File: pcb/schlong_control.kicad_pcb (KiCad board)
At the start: 2 copper layers, 50 x 50 mm, 37 parts, among them P1 Power Connector (120V AC), P2 Input, P3 Output, U1 74HC595, U2 MOC3063M, U3 MOC3063M, U4 MOC3063M, U5 MOC3063M, U6 MOC3063M, U7 LM7805

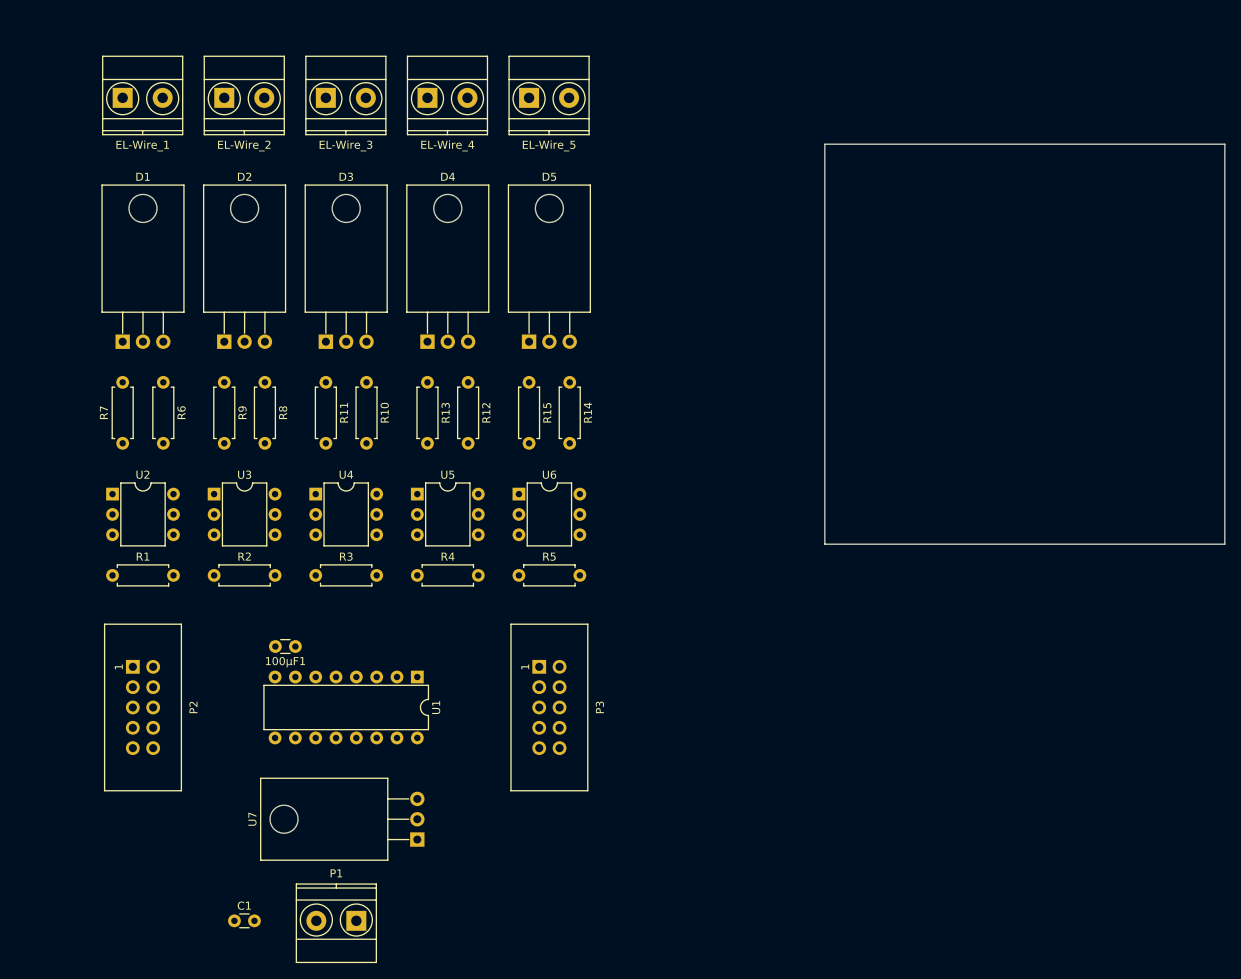
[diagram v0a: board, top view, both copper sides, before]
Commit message: make pcb more compact
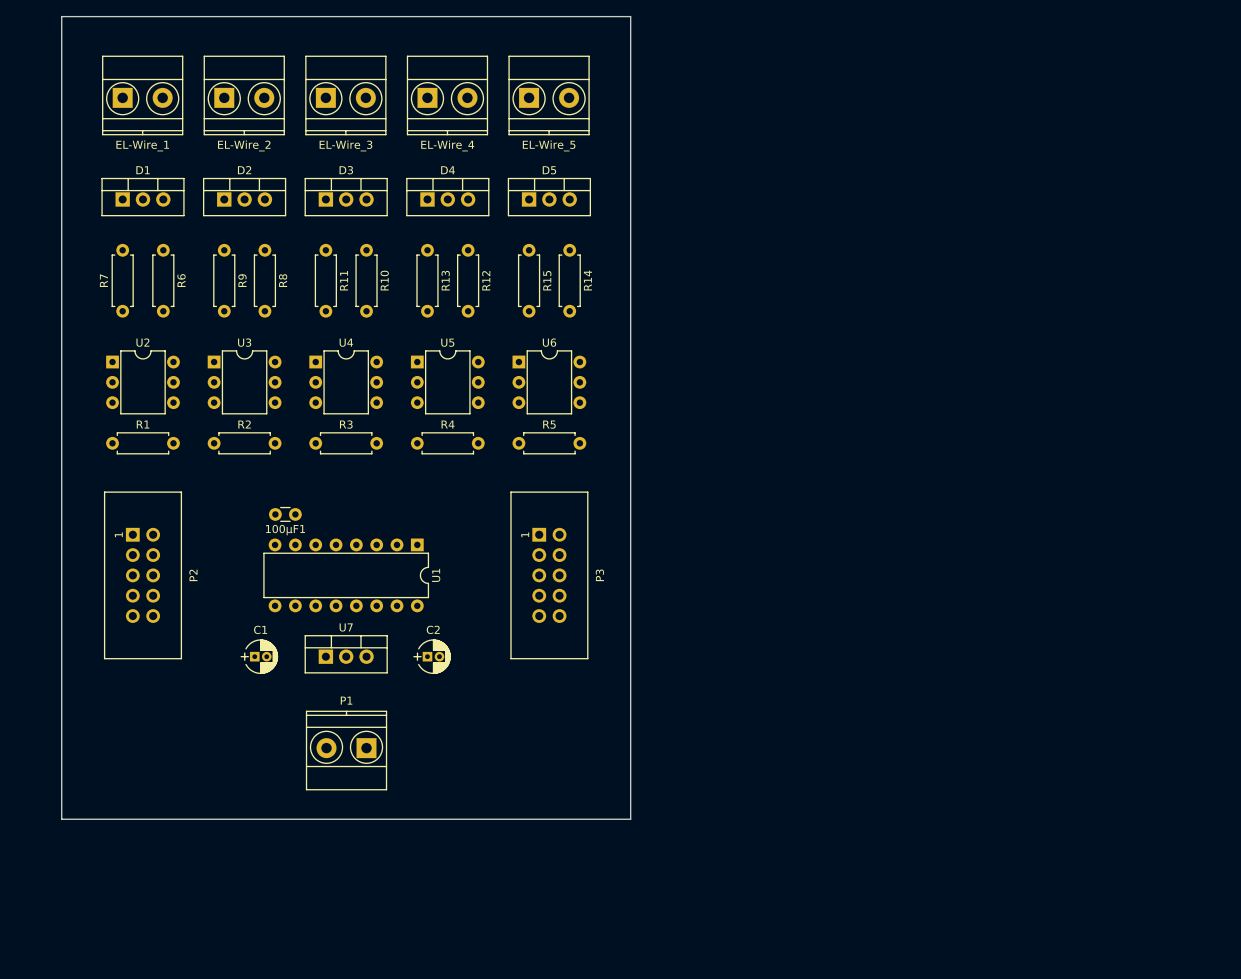
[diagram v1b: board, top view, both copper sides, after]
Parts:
- added C2: 0.1uF, Capacitors_THT:CP_Radial_D4.0mm_P1.50mm, F.Cu at (100.3, 99.1)
- C1: value 0.22µF -> 0.33µF; footprint Capacitors_THT:C_Disc_D3.0mm_W1.6mm_P2.50mm -> Capacitors_THT:CP_Radial_D4.0mm_P1.50mm
- D1, D2, D3, D4, D5, U7: footprint TO_SOT_Packages_THT:TO-220_Horizontal -> TO_SOT_Packages_THT:TO-220_Vertical
- moved C1 33.1 mm to (78.7, 99.1)
- moved U7 25.6 mm to (87.6, 99.1), turned to 0 degrees
- moved P1 21.6 mm to (92.7, 110.5)
- moved D1 17.8 mm to (62.2, 41.9)
- moved D2 17.8 mm to (74.9, 41.9)
- moved D3 17.8 mm to (87.6, 41.9)
- moved D4 17.8 mm to (100.3, 41.9)
- moved D5 17.8 mm to (113.0, 41.9)
- moved 100µF1 16.5 mm to (83.8, 81.3)
- moved P2 16.5 mm to (63.5, 83.8)
- moved P3 16.5 mm to (114.3, 83.8)
- moved R1 16.5 mm to (61.0, 72.4)
- moved R2 16.5 mm to (73.7, 72.4)
- moved R3 16.5 mm to (86.4, 72.4)
- moved R4 16.5 mm to (99.1, 72.4)
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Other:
- board size 50 x 50 mm -> 71.1 x 100.3 mm

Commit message: shinkify pcb even more + little fixes
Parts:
- EL-Wire_1, EL-Wire_2, EL-Wire_3, EL-Wire_4, EL-Wire_5: footprint Connectors_Terminal_Blocks:TerminalBlock_Pheonix_MKDS1.5-2pol -> Connectors:PINHEAD1-2
- moved C1 6.35 mm to (78.7, 92.7)
- moved C2 6.35 mm to (100.3, 92.7)
- moved U1 6.35 mm to (99.1, 78.7)
- moved U7 6.35 mm to (87.6, 92.7)
- moved R10 6.35 mm to (92.7, 41.9)
- moved R11 6.35 mm to (87.6, 41.9)
- moved R12 6.35 mm to (105.4, 41.9)
- moved R13 6.35 mm to (100.3, 41.9)
- moved R14 6.35 mm to (118.1, 41.9)
- moved R15 6.35 mm to (113.0, 41.9)
- moved R6 6.35 mm to (67.3, 41.9)
- moved R7 6.35 mm to (62.2, 49.5)
- moved R8 6.35 mm to (80.0, 41.9)
- moved R9 6.35 mm to (74.9, 41.9)
- moved 100µF1 6.35 mm to (83.8, 74.9)
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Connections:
- U1 pad 5: (no net) -> Net-(U1-Pad5)
- U1 pad 6: (no net) -> Net-(U1-Pad6)
- U1 pad 7: (no net) -> Net-(U1-Pad7)
- U2 pad 3: (no net) -> Net-(U2-Pad3)
- U2 pad 5: (no net) -> Net-(U2-Pad5)
- U3 pad 3: (no net) -> Net-(U3-Pad3)
- U3 pad 5: (no net) -> Net-(U3-Pad5)
- U4 pad 3: (no net) -> Net-(U4-Pad3)
- U4 pad 5: (no net) -> Net-(U4-Pad5)
- U5 pad 3: (no net) -> Net-(U5-Pad3)
- U5 pad 5: (no net) -> Net-(U5-Pad5)
- U6 pad 3: (no net) -> Net-(U6-Pad3)
- U6 pad 5: (no net) -> Net-(U6-Pad5)
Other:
- board size 71.1 x 100.3 mm -> 71.1 x 95.2 mm

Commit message: routed pcb
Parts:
- moved R7 7.53 mm to (62.2, 42.0), turned to 270 degrees
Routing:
- net /AC_P: track 0.00 -> 194.1 mm
- net /AC_N: track 0.00 -> 193.0 mm
- net GND: track 0.00 -> 182.4 mm
- net +12V: track 0.00 -> 81.3 mm
- net /SCK: track 0.00 -> 76.5 mm, vias 0 -> 4
- net /~LATCH: track 0.00 -> 58.4 mm, vias 0 -> 2
- net VCC: track 0.00 -> 54.6 mm
- net Net-(R1-Pad2): track 0.00 -> 40.4 mm
- net /~QH: track 0.00 -> 38.9 mm, vias 0 -> 2
- net Net-(R5-Pad2): track 0.00 -> 35.6 mm, vias 0 -> 1
- net /MOSI: track 0.00 -> 34.2 mm, vias 0 -> 1
- net Net-(D5-Pad3): track 0.00 -> 32.5 mm
- net Net-(D4-Pad3): track 0.00 -> 32.3 mm
- net Net-(D2-Pad3): track 0.00 -> 32.2 mm
- net Net-(D3-Pad3): track 0.00 -> 32.0 mm
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
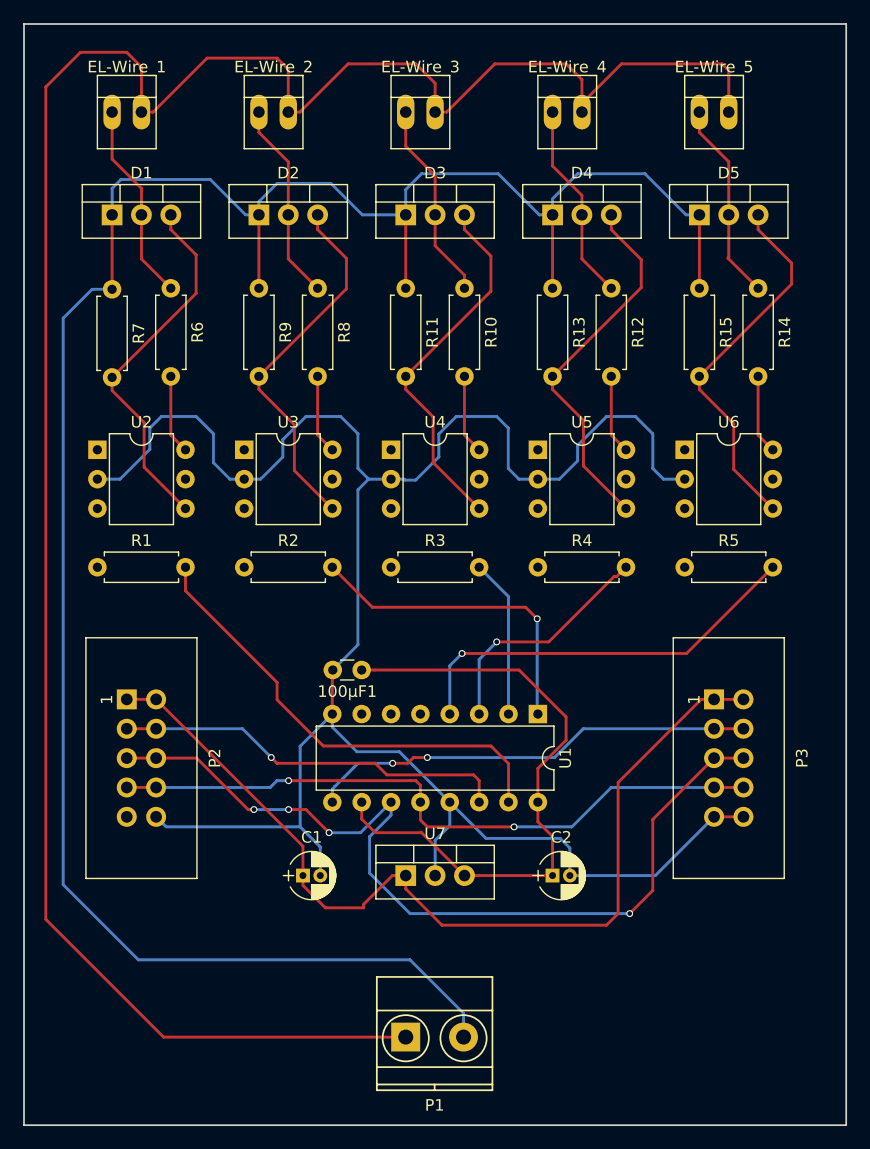
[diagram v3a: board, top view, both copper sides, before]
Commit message: redo routing (seperate logic voltage from AC voltage)
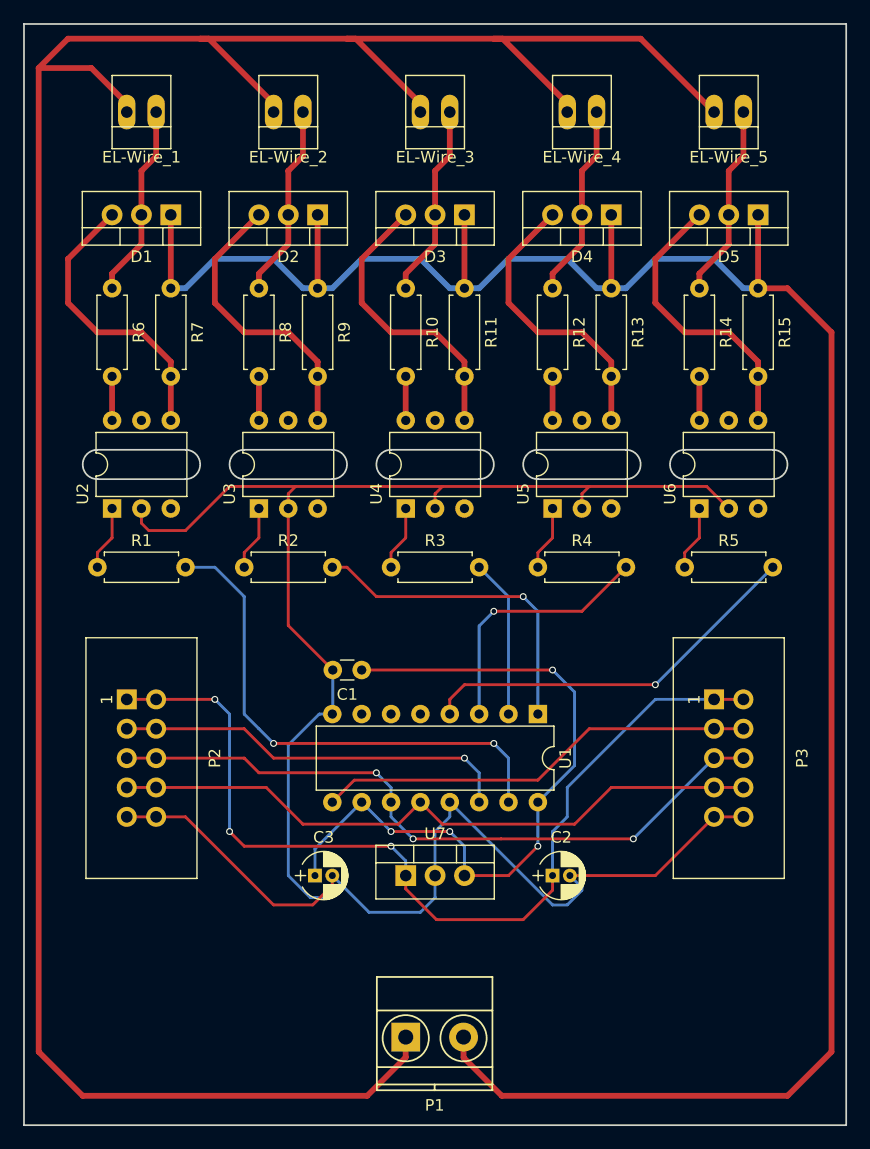
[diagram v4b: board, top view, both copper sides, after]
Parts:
- removed 100µF1: Bypass, Capacitors_THT:C_Disc_D3.0mm_W1.6mm_P2.50mm
- added C3: 0.1uF, Capacitors_ThroughHole:CP_Radial_D4.0mm_P1.50mm, F.Cu at (79.8, 92.7)
- C1: value 0.33µF -> 100nF; footprint Capacitors_THT:CP_Radial_D4.0mm_P1.50mm -> Capacitors_ThroughHole:C_Disc_D3.0mm_W1.6mm_P2.50mm
- C2: value 0.1uF -> 0.33µF; footprint Capacitors_THT:CP_Radial_D4.0mm_P1.50mm -> Capacitors_ThroughHole:CP_Radial_D4.0mm_P1.50mm
- moved C1 18.5 mm to (83.8, 74.9), turned to 180 degrees
- moved U3 5.24 mm to (74.9, 61.0), turned to 90 degrees
- moved U2 5.24 mm to (62.2, 61.0), turned to 90 degrees
- moved U4 5.24 mm to (87.6, 61.0), turned to 90 degrees
- moved U5 5.24 mm to (100.3, 61.0), turned to 90 degrees
- moved U6 5.24 mm to (113.0, 61.0), turned to 90 degrees
- moved R7 5.08 mm to (67.3, 41.9)
- moved D1 5.08 mm to (67.3, 35.6), turned to 180 degrees
- moved R6 5.08 mm to (62.2, 41.9)
- moved D2 5.08 mm to (80.0, 35.6), turned to 180 degrees
- moved D3 5.08 mm to (92.7, 35.6), turned to 180 degrees
- moved D4 5.08 mm to (105.4, 35.6), turned to 180 degrees
- moved D5 5.08 mm to (118.1, 35.6), turned to 180 degrees
- moved R10 5.08 mm to (87.6, 41.9)
- moved R11 5.08 mm to (92.7, 41.9)
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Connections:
- C1 pad 1: +12V -> VCC
- C2 pad 1: VCC -> +12V
- U1 pad 5: Net-(U1-Pad5) -> (no net)
- U1 pad 6: Net-(U1-Pad6) -> (no net)
- U1 pad 7: Net-(U1-Pad7) -> (no net)
- U2 pad 3: Net-(U2-Pad3) -> (no net)
- U2 pad 5: Net-(U2-Pad5) -> (no net)
- U3 pad 3: Net-(U3-Pad3) -> (no net)
- U3 pad 5: Net-(U3-Pad5) -> (no net)
- U4 pad 3: Net-(U4-Pad3) -> (no net)
- U4 pad 5: Net-(U4-Pad5) -> (no net)
- U5 pad 3: Net-(U5-Pad3) -> (no net)
- U5 pad 5: Net-(U5-Pad5) -> (no net)
- U6 pad 3: Net-(U6-Pad3) -> (no net)
- U6 pad 5: Net-(U6-Pad5) -> (no net)
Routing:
- net /AC_P: track 194.1 -> 221.5 mm
- net /SCK: track 76.5 -> 60.6 mm, vias 4 -> 3
- net VCC: track 54.6 -> 62.3 mm, vias 0 -> 4
- net Net-(D5-Pad3): track 32.5 -> 25.3 mm
- net Net-(D4-Pad3): track 32.3 -> 25.3 mm
- net Net-(D2-Pad3): track 32.2 -> 25.3 mm
- net Net-(D3-Pad3): track 32.0 -> 25.3 mm
- net Net-(D1-Pad3): track 31.9 -> 25.3 mm
- net /AC_N: track 193.0 -> 198.9 mm
- net Net-(R2-Pad1): track 0.00 -> 5.61 mm
- net Net-(R5-Pad1): track 0.00 -> 5.61 mm
- net Net-(R4-Pad1): track 0.00 -> 5.61 mm
- net Net-(R3-Pad1): track 0.00 -> 5.61 mm
- net Net-(R1-Pad1): track 0.00 -> 5.61 mm
- net Net-(R1-Pad2): track 40.4 -> 44.5 mm, vias 0 -> 2
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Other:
- outline, holes or cut-outs redrawn

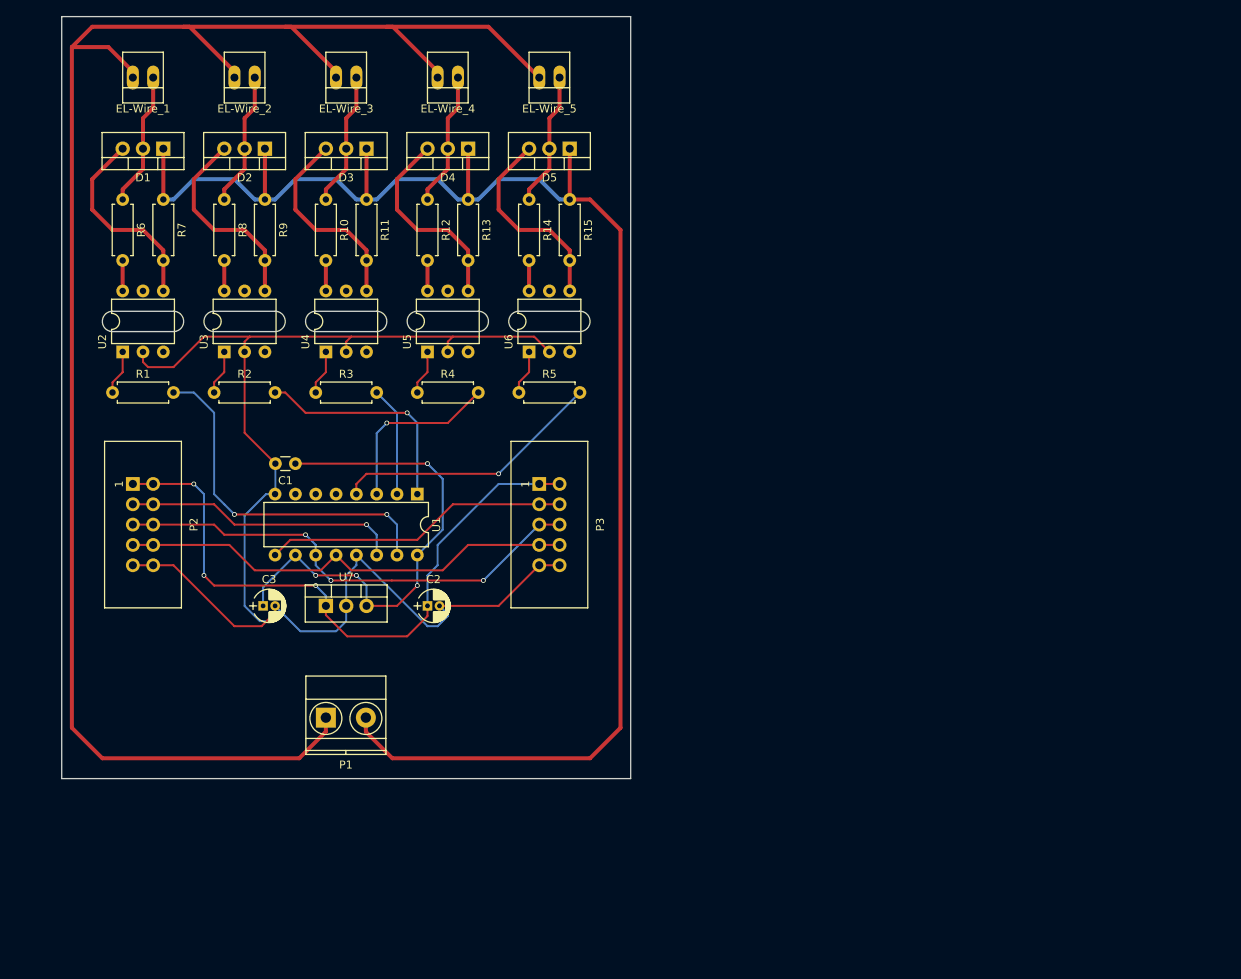
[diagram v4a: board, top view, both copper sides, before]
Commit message: pcb: improve seperation of low / high voltages
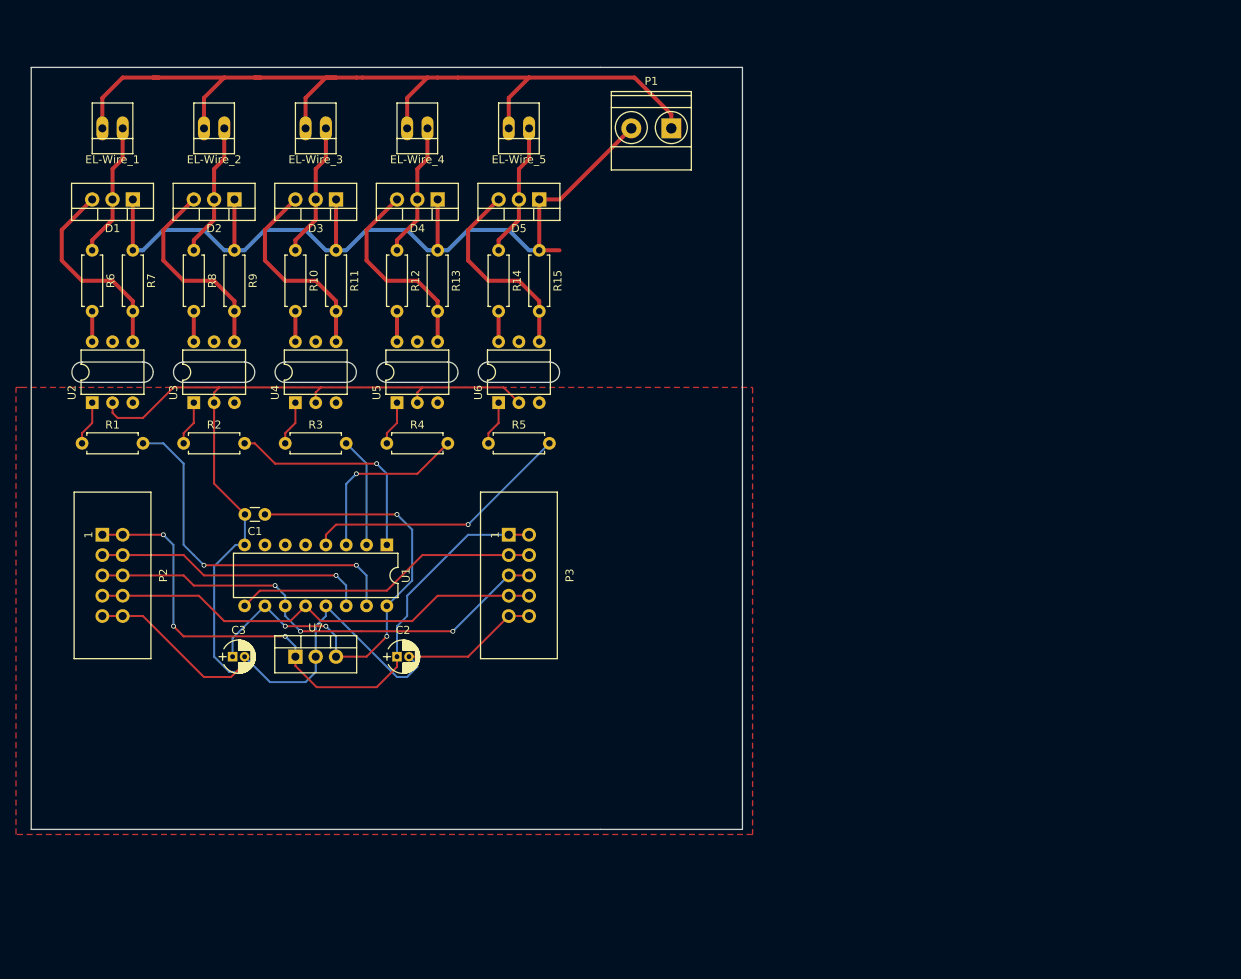
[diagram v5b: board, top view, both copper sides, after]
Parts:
- moved P1 85.4 mm to (130.8, 33.0), turned to 180 degrees
- moved C2 7.41 mm to (96.5, 99.1)
- moved C3 7.41 mm to (76.0, 99.1)
- moved U1 7.41 mm to (95.2, 85.1)
- moved U7 7.41 mm to (83.8, 99.1)
- moved EL-Wire_1 7.41 mm to (62.2, 33.0)
- moved EL-Wire_3 7.41 mm to (87.6, 33.0)
- moved EL-Wire_4 7.41 mm to (100.3, 33.0)
- moved EL-Wire_5 7.41 mm to (113.0, 33.0)
- moved R10 7.41 mm to (83.8, 48.3)
- moved R12 7.41 mm to (96.5, 48.3)
- moved R13 7.41 mm to (101.6, 48.3)
- moved R14 7.41 mm to (109.2, 48.3)
- moved R15 7.41 mm to (114.3, 48.3)
- moved R7 7.41 mm to (63.5, 48.3)
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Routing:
- net /AC_P: track 221.5 -> 115.0 mm
- net /AC_N: track 198.9 -> 108.7 mm
- added copper zone on F.Cu, net GND
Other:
- board size 71.1 x 95.2 mm -> 88.9 x 95.2 mm
